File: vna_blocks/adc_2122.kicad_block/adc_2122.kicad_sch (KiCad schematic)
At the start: 30 parts, among them U16 LTC2122IUK-TRPBF

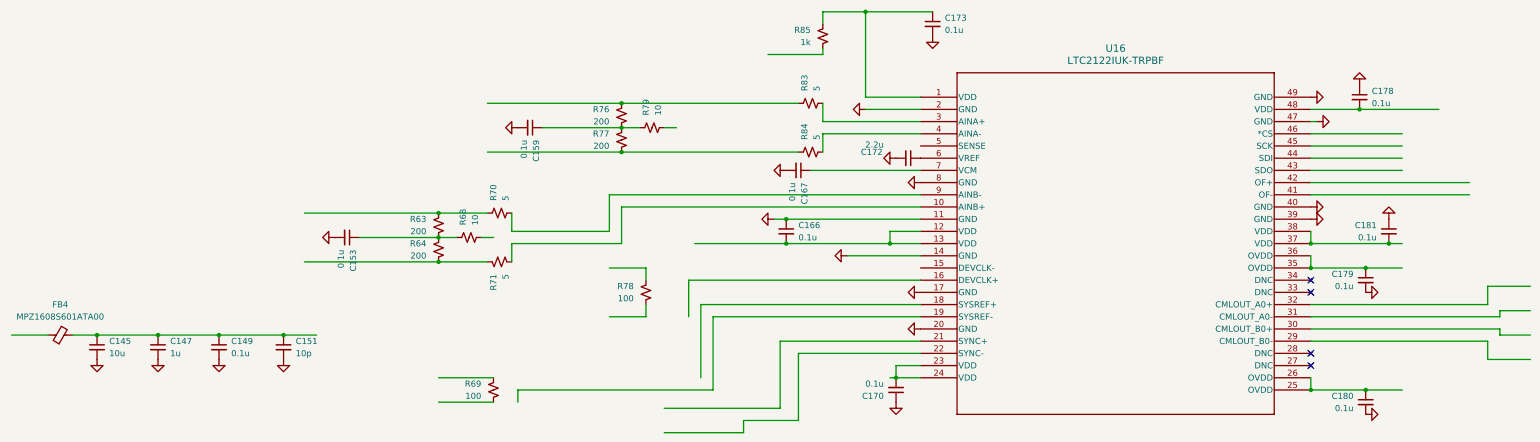
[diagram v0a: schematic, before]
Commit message: fixed IC courtyard issues
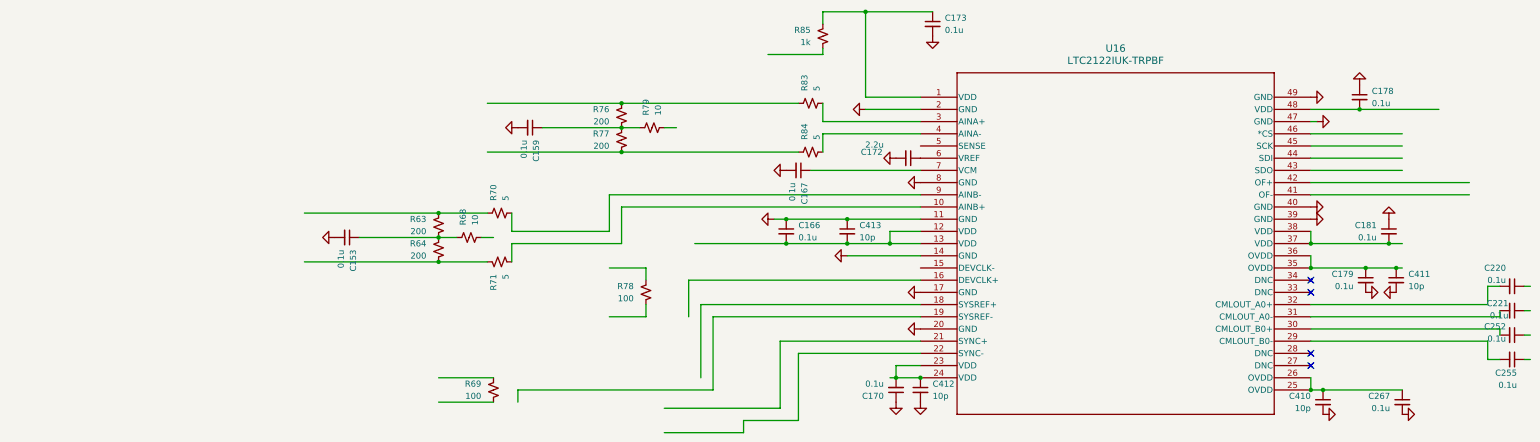
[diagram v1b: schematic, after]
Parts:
- removed C145: 10u, Capacitor_SMD:C_0402_1005Metric, symbol Device:C_Small
- removed C147: 1u, Capacitor_SMD:C_0402_1005Metric, symbol Device:C_Small
- removed C149, C180: 0.1u, Capacitor_SMD:C_0402_1005Metric, symbol Device:C_Small
- removed C151: 10p, Capacitor_SMD:C_0402_1005Metric, symbol Device:C_Small
- removed FB4: MPZ1608S601ATA00, Inductor_SMD:L_0603_1608Metric, symbol Device:FerriteBead_Small
- added C220, C221, C252, C255: 0.1u, Capacitor_SMD:C_0201_0603Metric, symbol Device:C_Small
- added C267: 0.1u, Capacitor_SMD:C_0402_1005Metric, symbol Device:C_Small
- added C410, C411, C412, C413: 10p, Capacitor_SMD:C_0201_0603Metric, symbol Device:C_Small
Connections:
- net GNDA: now also C267.2, C410.2, C411.2, C412.2, C413.1
- net at C170.2, U16.23 (VDD), U16.24 (VDD): now also C412.1
- net at C166.2, U16.12 (VDD), U16.13 (VDD): now also C413.2
- net at C179.1, U16.35 (OVDD), U16.36 (OVDD): now also C411.1
- net at U16.25 (OVDD), U16.26 (OVDD): now also C267.1, C410.1
- net at U16.29 (CMLOUT_B0-): now also C255.2
- net at U16.30 (CMLOUT_B0+): now also C252.2
- net at U16.31 (CMLOUT_A0-): now also C221.2
- net at U16.32 (CMLOUT_A0+): now also C220.2
